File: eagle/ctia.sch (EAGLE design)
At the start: 6 parts, among them IC1 IVC102UADAPTOR

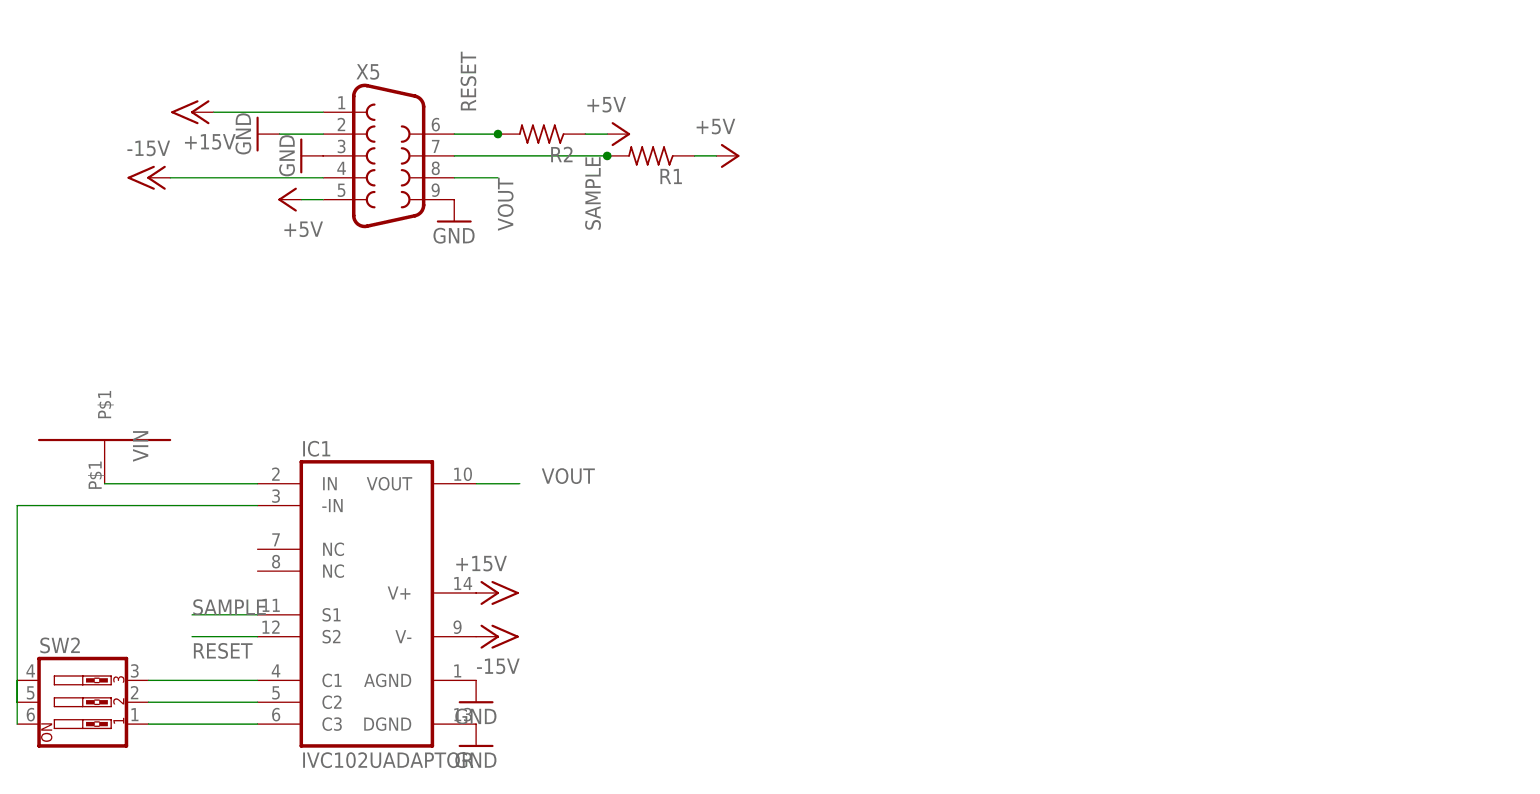
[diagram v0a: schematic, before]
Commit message: flange alone board for test
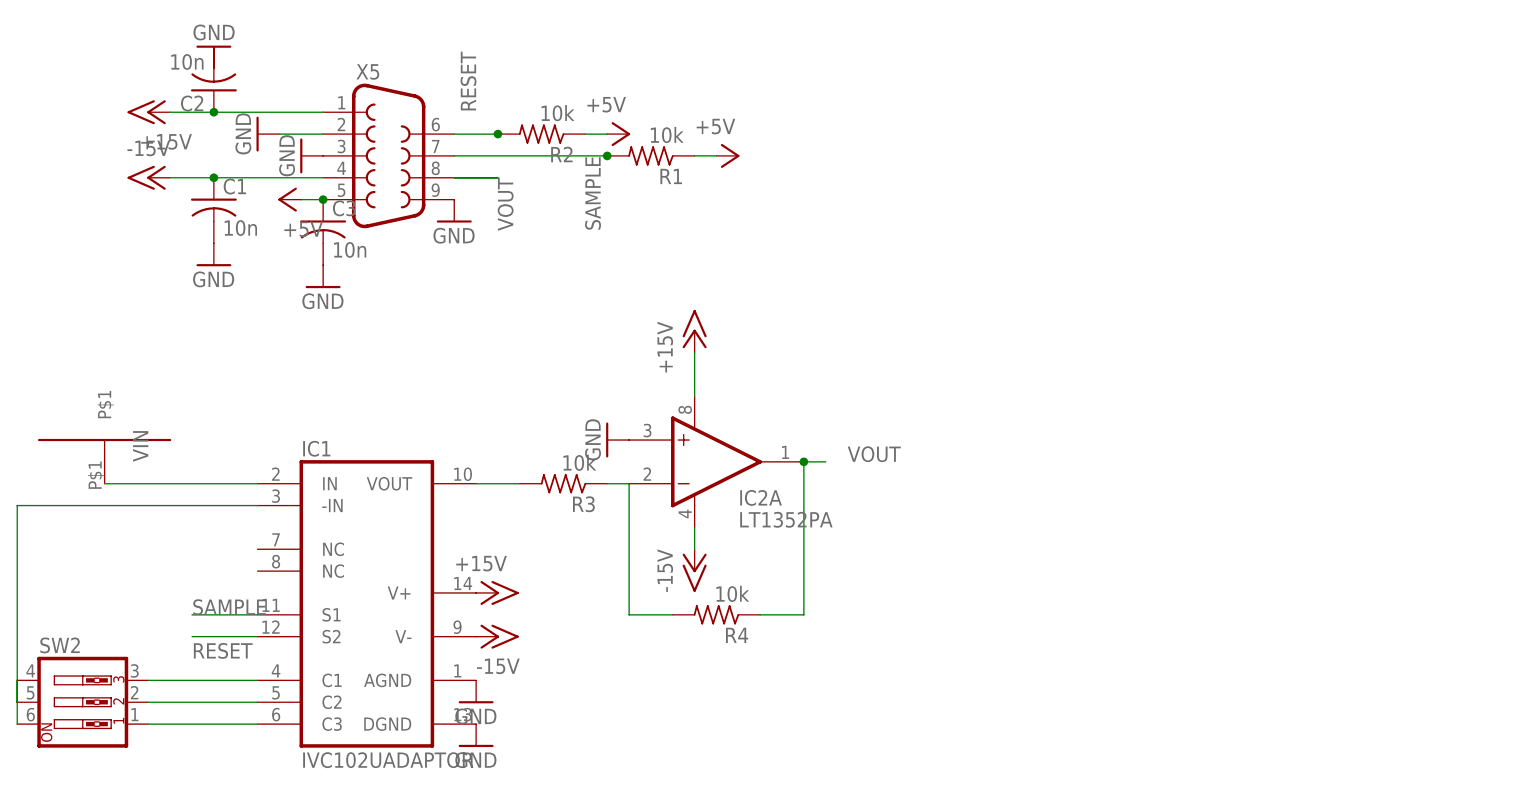
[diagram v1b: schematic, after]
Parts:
- added C1, C2, C3: 10n, rcl:C-US050-050X075
- added IC2: LT1352PA, linear-technology:LT1352PA
- added R3, R4: 10k, resistor:R-US_0207/10
- R1: value (none) -> 10k; device resistor:R-US_0207/12 -> resistor:R-US_0207/15
- R2: value (none) -> 10k; device resistor:R-US_0207/10 -> resistor:R-US_0207/15
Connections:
- new net N$5: IC1.VOUT, R3.2
- new net N$6: IC2A.-IN, R3.1, R4.2
- net +15V: now also C2.1, IC2A.V+
- net +5V: now also C3.1
- net -15V: now also C1.1, IC2A.V-
- net GND: now also C1.2, C3.2, IC2A.+IN
- net VOUT: now also IC2A.OUT, R4.1; no longer IC1.VOUT

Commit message: zener protect
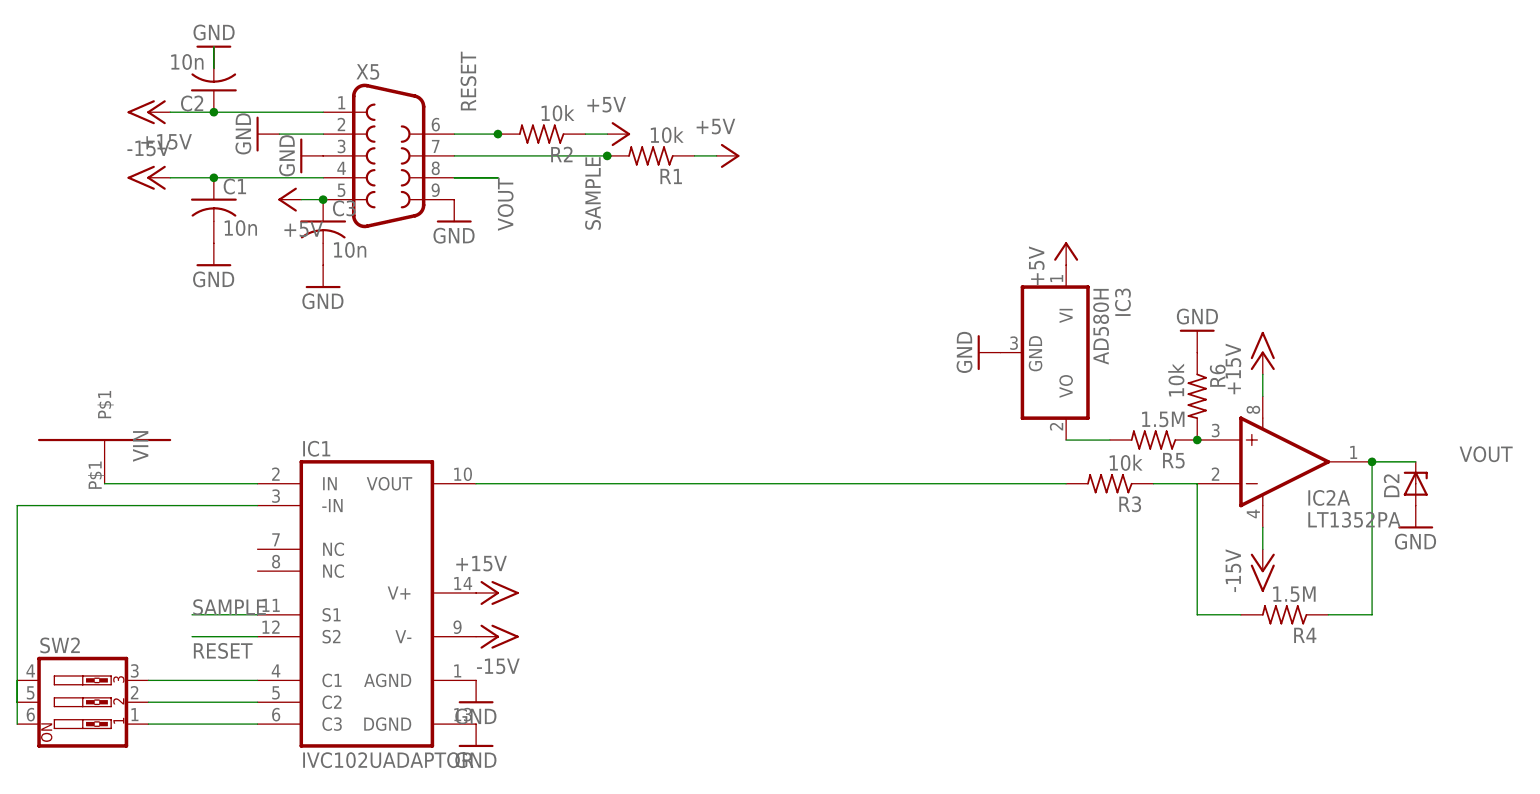
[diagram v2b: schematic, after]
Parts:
- added D2: (no value), diode:ZENER-DIODEDO41Z10
- added IC3: AD580H, linear:AD580H
- added R5: 1.5M, resistor:R-US_0207/10
- added R6: 10k, resistor:R-US_0207/10
- R4: value 10k -> 1.5M
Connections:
- new net N$7: IC2A.+IN, R5.1, R6.2
- new net N$8: IC3.VO, R5.2
- net +5V: now also IC3.VI
- net GND: now also C2.2, D2.A, IC3.GND, R6.1; no longer IC2A.+IN
- net VOUT: now also D2.C
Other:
- moved on the sheet: IC2A, R3, R4

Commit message: lower noise
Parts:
- added R7: 10k, pot:TRIM_US-B64Y
- IC2: value LT1352PA -> OPA27GP; device linear-technology:LT1352PA -> linear:OPA27GP
- R3, R6: value 10k -> 1M
- R4, R5: value 1.5M -> 1M
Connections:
- new net N$10: IC2.OFF2, R7.A
- new net N$9: IC2.OFF1, R7.E
- net +15V: now also IC2.V+, R7.S; no longer IC2A.V+
- net -15V: now also IC2.V-; no longer IC2A.V-
- net N$6: now also IC2.-IN; no longer IC2A.-IN
- net N$7: now also IC2.+IN; no longer IC2A.+IN
- net VOUT: now also IC2.OUT; no longer IC2A.OUT
